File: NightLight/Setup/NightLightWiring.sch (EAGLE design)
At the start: 19 parts

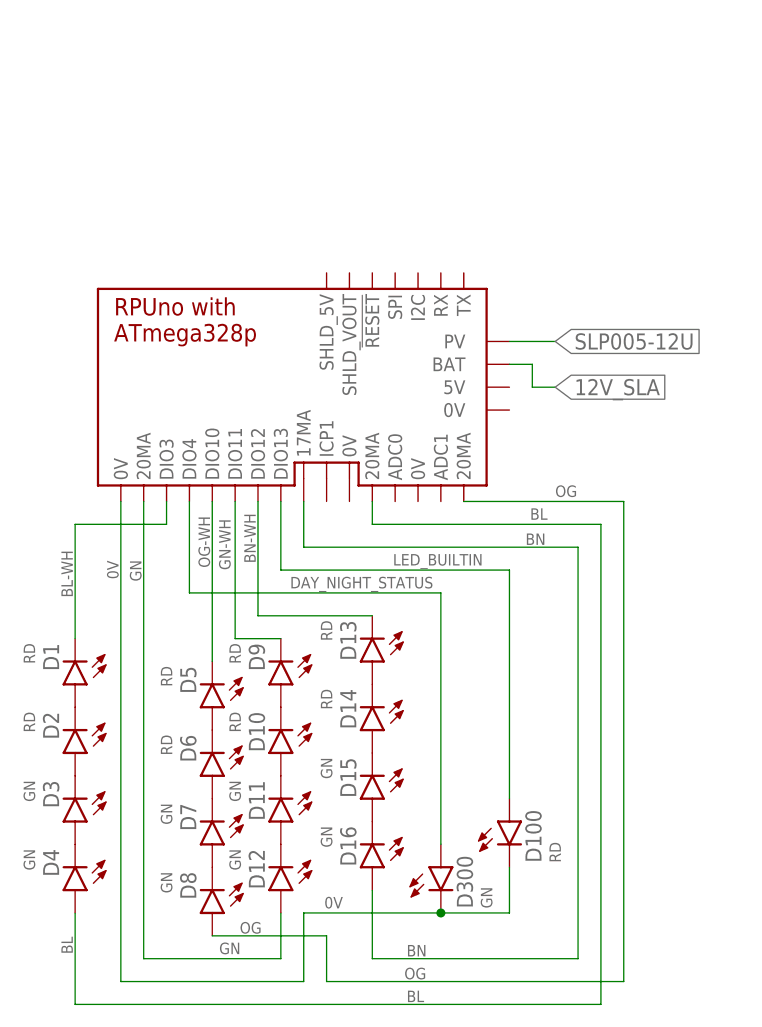
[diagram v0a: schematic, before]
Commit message: NightLight: evaluation
100 Ohm added to status led
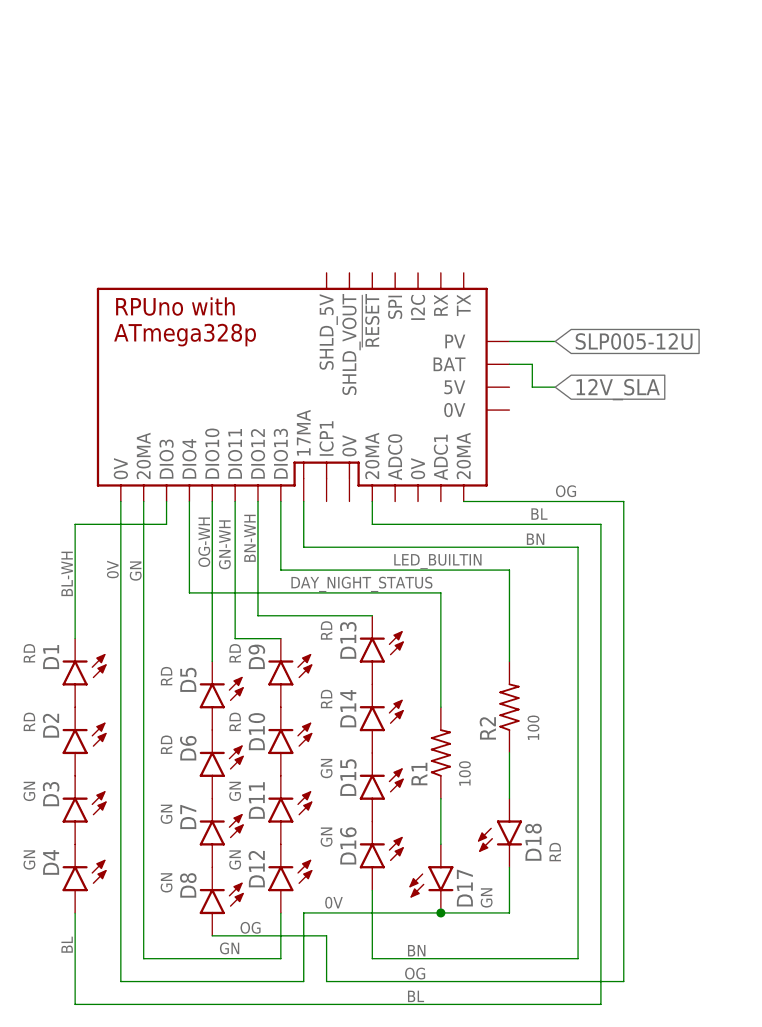
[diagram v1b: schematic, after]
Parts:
- added R1, R2: 100, R-C:R0805
- renumbered D100 to D18, D300 to D17
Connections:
- new net N$1: D17.A, R1.1
- new net N$2: D18.A, R2.1
- net DAY_NIGHT_STATUS: now also R1.2; no longer D17.A
- net LED_BUILTIN: now also R2.2; no longer D18.A
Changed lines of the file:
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@@
 <parts>
 <part name="BM3" library="Documentation" deviceset="RPUNO" device=""/>
-<part name="D100" library="D-LED" deviceset="LED" device="5MM" value="RD"/>
-<part name="D300" library="D-LED" deviceset="LED" device="5MM" value="GN"/>
+<part name="D18" library="D-LED" deviceset="LED" device="5MM" value="RD"/>
+<part name="D17" library="D-LED" deviceset="LED" device="5MM" value="GN"/>
 <part name="D1" library="D-LED" deviceset="LED" device="5MM" value="RD"/>
 <part name="D2" library="D-LED" deviceset="LED" device="5MM" value="RD"/>
@@
 <part name="D15" library="D-LED" deviceset="LED" device="5MM" value="GN"/>
 <part name="D16" library="D-LED" deviceset="LED" device="5MM" value="GN"/>
+<part name="R1" library="R-C" deviceset="R" device="0805" value="100"/>
+<part name="R2" library="R-C" deviceset="R" device="0805" value="100"/>
 </parts>
 <sheets>
@@
 <instances>
 <instance part="BM3" gate="G$1" x="45.72" y="109.22"/>
-<instance part="D100" gate="G$1" x="66.04" y="58.42"/>
-<instance part="D300" gate="G$1" x="58.42" y="53.34"/>
+<instance part="D18" gate="G$1" x="66.04" y="58.42"/>
+<instance part="D17" gate="G$1" x="58.42" y="53.34"/>
 <instance part="D1" gate="G$1" x="17.78" y="73.66" rot="R180"/>
 <instance part="D2" gate="G$1" x="17.78" y="66.04" rot="R180"/>
@@
 <instance part="D15" gate="G$1" x="50.8" y="60.96" rot="R180"/>
 <instance part="D16" gate="G$1" x="50.8" y="53.34" rot="R180"/>
+<instance part="R1" gate="G$1" x="58.42" y="66.04" rot="R90"/>
+<instance part="R2" gate="G$1" x="66.04" y="71.12" rot="R90"/>
 </instances>
 <busses>
@@
 <segment>
 <pinref part="BM3" gate="G$1" pin="DIO4"/>
-<wire x1="58.42" y1="55.88" x2="58.42" y2="83.82" width="0.1524" layer="91"/>
+<wire x1="58.42" y1="71.12" x2="58.42" y2="83.82" width="0.1524" layer="91"/>
 <wire x1="58.42" y1="83.82" x2="30.48" y2="83.82" width="0.1524" layer="91"/>
 <wire x1="30.48" y1="83.82" x2="30.48" y2="93.98" width="0.1524" layer="91"/>
-<pinref part="D300" gate="G$1" pin="A"/>
 <label x="41.656" y="84.328" size="1.27" layer="91"/>
+<pinref part="R1" gate="G$1" pin="2"/>
 </segment>
 </net>
@@
 <segment>
 <pinref part="BM3" gate="G$1" pin="DIO13"/>
-<pinref part="D100" gate="G$1" pin="A"/>
 <wire x1="40.64" y1="93.98" x2="40.64" y2="86.36" width="0.1524" layer="91"/>
 <wire x1="40.64" y1="86.36" x2="66.04" y2="86.36" width="0.1524" layer="91"/>
-<wire x1="66.04" y1="86.36" x2="66.04" y2="60.96" width="0.1524" layer="91"/>
+<wire x1="66.04" y1="86.36" x2="66.04" y2="76.2" width="0.1524" layer="91"/>
 <label x="53.086" y="86.868" size="1.27" layer="91"/>
+<pinref part="R2" gate="G$1" pin="2"/>
 </segment>
 </net>
 <net name="0V" class="0">
 <segment>
-<pinref part="D100" gate="G$1" pin="K"/>
+<pinref part="D18" gate="G$1" pin="K"/>
 <wire x1="66.04" y1="53.34" x2="66.04" y2="48.26" width="0.1524" layer="91"/>
 <wire x1="66.04" y1="48.26" x2="58.42" y2="48.26" width="0.1524" layer="91"/>
-<pinref part="D300" gate="G$1" pin="K"/>
+<pinref part="D17" gate="G$1" pin="K"/>
 <pinref part="BM3" gate="G$1" pin="0V@3"/>
 <wire x1="22.86" y1="93.98" x2="22.86" y2="40.64" width="0.1524" layer="91"/>
@@
 </segment>
 </net>
+<net name="N$1" class="0">
+<segment>
+<pinref part="D17" gate="G$1" pin="A"/>
+<pinref part="R1" gate="G$1" pin="1"/>
+<wire x1="58.42" y1="60.96" x2="58.42" y2="55.88" width="0.1524" layer="91"/>
+</segment>
+</net>
+<net name="N$2" class="0">
+<segment>
+<pinref part="D18" gate="G$1" pin="A"/>
+<pinref part="R2" gate="G$1" pin="1"/>
+<wire x1="66.04" y1="66.04" x2="66.04" y2="60.96" width="0.1524" layer="91"/>
+</segment>
+</net>

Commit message: NightLight: ^9 updates
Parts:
- removed R1, R2: 100, R-C:R0805
- added D19: RD, D-LED:LED5MM
- D11, D12, D15, D16, D3, D4, D7, D8: value GN -> RD
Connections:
- removed net DAY_NIGHT_STATUS: BM3.DIO4, R1.2
- removed net LED_BUILTIN: BM3.DIO13, R2.2
- removed net N$1: D17.A, R1.1
- removed net N$2: D18.A, R2.1
- new net DAYNIGHT_STATUS_LED: BM3.DIO12, D17.A
- new net LIGHT_SENSOR: BM3.ADC2_16, D19.K
- new net STATUS_LED: BM3.DIO13, D18.A
- net 0V: no longer BM3.0V@3
- net 12V_SLA: now also BM3.PWR; no longer BM3.BAT
- net BL: now also BM3.CS0_EN5; no longer BM3.20MA@0
- net BL-WH: now also BM3.0V@3; no longer BM3.DIO3
- net BN: now also BM3.CS3_EN4; no longer BM3.17MA@0
- net BN-WH: now also BM3.0V@6; no longer BM3.DIO12
- net GN: now also BM3.CS2_EN3; no longer BM3.20MA@2
- net GN-WH: now also BM3.0V@5, D19.A; no longer BM3.DIO11
- net OG: now also BM3.CS1_EN6; no longer BM3.20MA@1
- net OG-WH: no longer BM3.DIO10
- net SLP005-12U: now also BM3.ALT; no longer BM3.PV
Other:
- moved on the sheet: D1, D10, D11, D12, D13, D14, D15, D16, D17, D18, D2, D3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

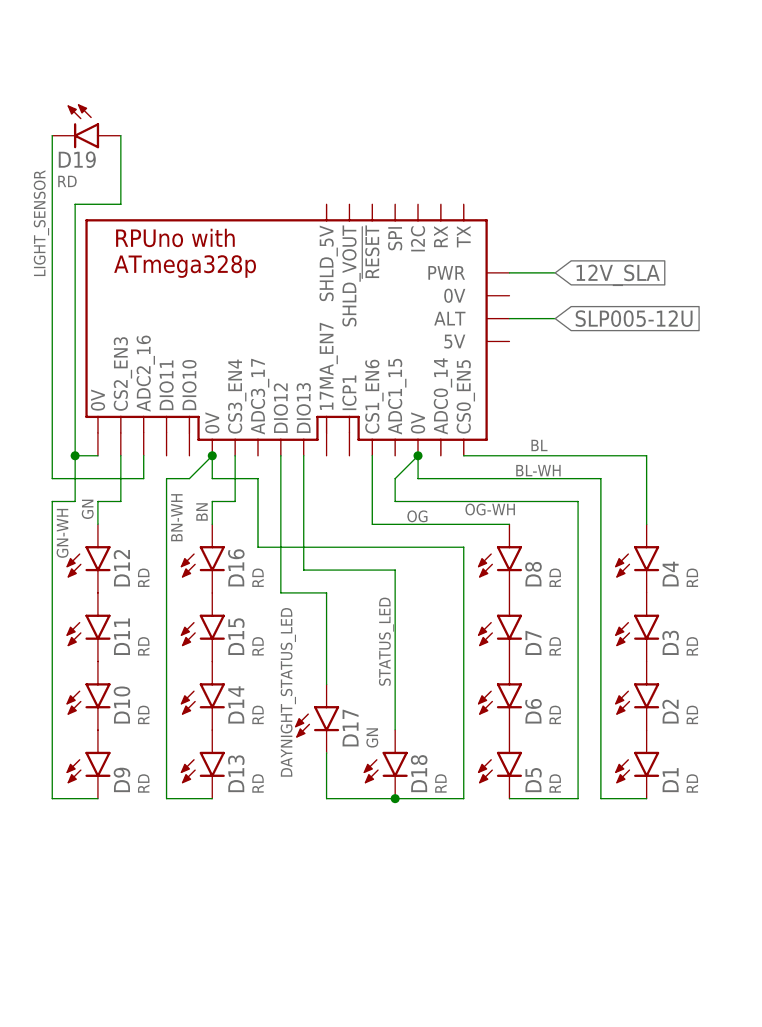
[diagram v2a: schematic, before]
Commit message: Reflow: ^9 updates and add a light sensor to start profile
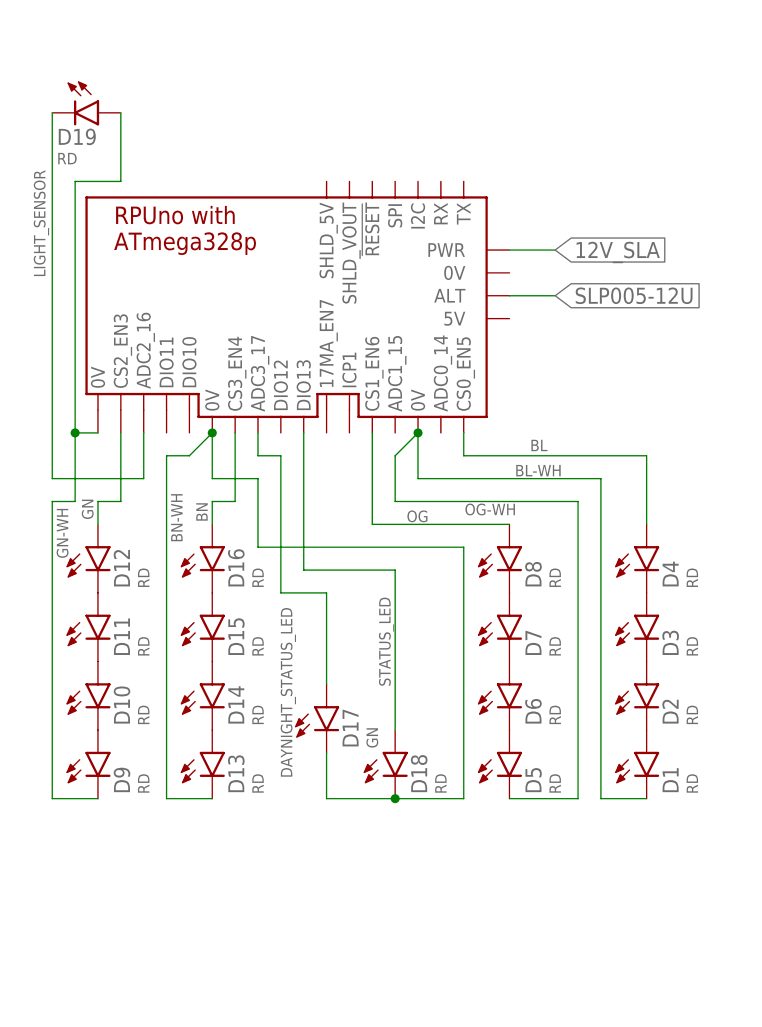
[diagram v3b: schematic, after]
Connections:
- net DAYNIGHT_STATUS_LED: now also BM3.ADC3_17; no longer BM3.DIO12
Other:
- moved on the sheet: D19
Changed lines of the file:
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@@
 </plain>
 <instances>
-<instance part="BM3" gate="G$1" x="45.72" y="114.3"/>
+<instance part="BM3" gate="G$1" x="45.72" y="116.84"/>
 <instance part="D18" gate="G$1" x="53.34" y="66.04"/>
 <instance part="D17" gate="G$1" x="45.72" y="71.12"/>
@@
 <instance part="D15" gate="G$1" x="33.02" y="81.28"/>
 <instance part="D16" gate="G$1" x="33.02" y="88.9"/>
-<instance part="D19" gate="G$1" x="20.32" y="134.62" rot="R270"/>
+<instance part="D19" gate="G$1" x="20.32" y="137.16" rot="R270"/>
 </instances>
 <busses>
@@
 <net name="SLP005-12U" class="0">
 <segment>
-<label x="71.12" y="114.3" size="1.778" layer="91" xref="yes"/>
+<label x="71.12" y="116.84" size="1.778" layer="91" xref="yes"/>
 <pinref part="BM3" gate="G$1" pin="ALT"/>
-<wire x1="71.12" y1="114.3" x2="66.04" y2="114.3" width="0.1524" layer="91"/>
+<wire x1="71.12" y1="116.84" x2="66.04" y2="116.84" width="0.1524" layer="91"/>
 </segment>
 </net>
 <net name="12V_SLA" class="0">
 <segment>
-<label x="71.12" y="119.38" size="1.778" layer="91" xref="yes"/>
+<label x="71.12" y="121.92" size="1.778" layer="91" xref="yes"/>
 <pinref part="BM3" gate="G$1" pin="PWR"/>
-<wire x1="71.12" y1="119.38" x2="66.04" y2="119.38" width="0.1524" layer="91"/>
+<wire x1="71.12" y1="121.92" x2="66.04" y2="121.92" width="0.1524" layer="91"/>
 </segment>
 </net>
@@
 <wire x1="40.64" y1="83.82" x2="40.64" y2="99.06" width="0.1524" layer="91"/>
 <label x="41.91" y="63.246" size="1.27" layer="91" rot="R90"/>
-<pinref part="BM3" gate="G$1" pin="DIO12"/>
 <pinref part="D17" gate="G$1" pin="A"/>
+<pinref part="BM3" gate="G$1" pin="ADC3_17"/>
+<wire x1="38.1" y1="101.6" x2="38.1" y2="99.06" width="0.1524" layer="91"/>
+<wire x1="38.1" y1="99.06" x2="40.64" y2="99.06" width="0.1524" layer="91"/>
 </segment>
 </net>
@@
 <label x="52.832" y="73.406" size="1.27" layer="91" rot="R90"/>
 <pinref part="BM3" gate="G$1" pin="DIO13"/>
-<wire x1="43.18" y1="86.36" x2="43.18" y2="99.06" width="0.1524" layer="91"/>
+<wire x1="43.18" y1="86.36" x2="43.18" y2="101.6" width="0.1524" layer="91"/>
 <pinref part="D18" gate="G$1" pin="A"/>
 </segment>
@@
 <wire x1="38.1" y1="88.9" x2="38.1" y2="96.52" width="0.1524" layer="91"/>
 <wire x1="38.1" y1="96.52" x2="33.02" y2="96.52" width="0.1524" layer="91"/>
-<wire x1="33.02" y1="96.52" x2="33.02" y2="98.552" width="0.1524" layer="91"/>
+<wire x1="33.02" y1="96.52" x2="33.02" y2="101.092" width="0.1524" layer="91"/>
 </segment>
 </net>
@@
 <pinref part="BM3" gate="G$1" pin="0V@3"/>
 <wire x1="76.2" y1="96.52" x2="55.88" y2="96.52" width="0.1524" layer="91"/>
-<wire x1="55.88" y1="96.52" x2="55.88" y2="99.06" width="0.1524" layer="91"/>
-<wire x1="55.88" y1="99.06" x2="55.626" y2="99.06" width="0.1524" layer="91"/>
-<junction x="55.88" y="99.06"/>
+<wire x1="55.88" y1="96.52" x2="55.88" y2="101.6" width="0.1524" layer="91"/>
+<wire x1="55.88" y1="101.6" x2="55.626" y2="101.6" width="0.1524" layer="91"/>
+<junction x="55.88" y="101.6"/>
 </segment>
 </net>
@@
 <wire x1="81.28" y1="91.44" x2="81.28" y2="99.06" width="0.1524" layer="91"/>
 <wire x1="81.28" y1="99.06" x2="60.96" y2="99.06" width="0.1524" layer="91"/>
+<wire x1="60.96" y1="99.06" x2="60.96" y2="101.6" width="0.1524" layer="91"/>
 <label x="68.326" y="99.568" size="1.27" layer="91"/>
 <pinref part="BM3" gate="G$1" pin="CS0_EN5"/>
@@
 <wire x1="73.66" y1="60.96" x2="73.66" y2="93.98" width="0.1524" layer="91"/>
 <wire x1="73.66" y1="93.98" x2="53.34" y2="93.98" width="0.1524" layer="91"/>
-<wire x1="53.34" y1="93.98" x2="53.34" y2="96.52" width="0.1524" layer="91"/>
-<wire x1="53.34" y1="96.52" x2="55.626" y2="98.806" width="0.1524" layer="91"/>
+<wire x1="53.34" y1="93.98" x2="53.34" y2="99.06" width="0.1524" layer="91"/>
+<wire x1="53.34" y1="99.06" x2="55.626" y2="101.346" width="0.1524" layer="91"/>
 </segment>
 </net>
@@
 <pinref part="BM3" gate="G$1" pin="CS1_EN6"/>
 <wire x1="66.04" y1="91.44" x2="50.8" y2="91.44" width="0.1524" layer="91"/>
-<wire x1="50.8" y1="91.44" x2="50.8" y2="99.06" width="0.1524" layer="91"/>
+<wire x1="50.8" y1="91.44" x2="50.8" y2="101.6" width="0.1524" layer="91"/>
 </segment>
 </net>
@@
 <wire x1="15.24" y1="60.96" x2="15.24" y2="93.98" width="0.1524" layer="91"/>
 <wire x1="15.24" y1="93.98" x2="17.78" y2="93.98" width="0.1524" layer="91"/>
-<wire x1="17.78" y1="93.98" x2="17.78" y2="99.06" width="0.1524" layer="91"/>
+<wire x1="17.78" y1="93.98" x2="17.78" y2="101.6" width="0.1524" layer="91"/>
 <pinref part="BM3" gate="G$1" pin="0V@5"/>
-<wire x1="17.78" y1="99.06" x2="20.32" y2="99.06" width="0.1524" layer="91"/>
+<wire x1="17.78" y1="101.6" x2="20.32" y2="101.6" width="0.1524" layer="91"/>
 <pinref part="D19" gate="G$1" pin="A"/>
-<wire x1="22.86" y1="134.62" x2="22.86" y2="127" width="0.1524" layer="91"/>
-<wire x1="22.86" y1="127" x2="17.78" y2="127" width="0.1524" layer="91"/>
-<wire x1="17.78" y1="127" x2="17.78" y2="99.06" width="0.1524" layer="91"/>
-<junction x="17.78" y="99.06"/>
+<wire x1="22.86" y1="137.16" x2="22.86" y2="129.54" width="0.1524" layer="91"/>
+<wire x1="22.86" y1="129.54" x2="17.78" y2="129.54" width="0.1524" layer="91"/>
+<wire x1="17.78" y1="129.54" x2="17.78" y2="101.6" width="0.1524" layer="91"/>
+<junction x="17.78" y="101.6"/>
 </segment>
 </net>
@@
 <wire x1="33.02" y1="60.96" x2="27.94" y2="60.96" width="0.1524" layer="91"/>
 <label x="29.718" y="89.408" size="1.27" layer="91" rot="R90"/>
-<wire x1="27.94" y1="60.96" x2="27.94" y2="96.52" width="0.1524" layer="91"/>
-<wire x1="27.94" y1="96.52" x2="30.48" y2="96.52" width="0.1524" layer="91"/>
+<wire x1="27.94" y1="60.96" x2="27.94" y2="99.06" width="0.1524" layer="91"/>
+<wire x1="27.94" y1="99.06" x2="30.48" y2="99.06" width="0.1524" layer="91"/>
 <pinref part="BM3" gate="G$1" pin="0V@6"/>
-<wire x1="30.48" y1="96.52" x2="33.02" y2="99.06" width="0.1524" layer="91"/>
-<wire x1="33.02" y1="99.06" x2="33.274" y2="99.06" width="0.1524" layer="91"/>
-<junction x="33.02" y="99.06"/>
+<wire x1="30.48" y1="99.06" x2="33.02" y2="101.6" width="0.1524" layer="91"/>
+<wire x1="33.02" y1="101.6" x2="33.274" y2="101.6" width="0.1524" layer="91"/>
+<junction x="33.02" y="101.6"/>
 </segment>
 </net>
@@
 <segment>
 <pinref part="D12" gate="G$1" pin="A"/>
-<wire x1="22.86" y1="99.06" x2="22.86" y2="93.98" width="0.1524" layer="91"/>
+<wire x1="22.86" y1="101.6" x2="22.86" y2="93.98" width="0.1524" layer="91"/>
 <wire x1="22.86" y1="93.98" x2="20.32" y2="93.98" width="0.1524" layer="91"/>
 <wire x1="20.32" y1="93.98" x2="20.32" y2="91.44" width="0.1524" layer="91"/>
@@
 <wire x1="33.02" y1="91.44" x2="33.02" y2="93.98" width="0.1524" layer="91"/>
 <wire x1="33.02" y1="93.98" x2="35.56" y2="93.98" width="0.1524" layer="91"/>
-<wire x1="35.56" y1="93.98" x2="35.56" y2="99.06" width="0.1524" layer="91"/>
+<wire x1="35.56" y1="93.98" x2="35.56" y2="101.6" width="0.1524" layer="91"/>
 <label x="32.512" y="91.694" size="1.27" layer="91" rot="R90"/>
 <pinref part="BM3" gate="G$1" pin="CS3_EN4"/>
@@
 <segment>
 <pinref part="D19" gate="G$1" pin="K"/>
-<wire x1="15.24" y1="134.62" x2="15.24" y2="96.52" width="0.1524" layer="91"/>
+<wire x1="15.24" y1="137.16" x2="15.24" y2="96.52" width="0.1524" layer="91"/>
 <wire x1="15.24" y1="96.52" x2="25.4" y2="96.52" width="0.1524" layer="91"/>
 <pinref part="BM3" gate="G$1" pin="ADC2_16"/>
-<wire x1="25.4" y1="96.52" x2="25.4" y2="99.06" width="0.1524" layer="91"/>
+<wire x1="25.4" y1="96.52" x2="25.4" y2="101.6" width="0.1524" layer="91"/>
 <label x="14.478" y="118.872" size="1.27" layer="91" rot="R90"/>
 </segment>

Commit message: Solenoid: wiring show flow sensor
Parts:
- added R1: 100k, R-C:R0805
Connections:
- net GN-WH: now also R1.1
- net LIGHT_SENSOR: now also R1.2
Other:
- moved on the sheet: D19
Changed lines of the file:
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@@
 <part name="D16" library="D-LED" deviceset="LED" device="5MM" value="RD"/>
 <part name="D19" library="D-LED" deviceset="LED" device="5MM" value="RD"/>
+<part name="R1" library="R-C" deviceset="R" device="0805" value="100k"/>
 </parts>
 <sheets>
@@
 <instance part="D15" gate="G$1" x="33.02" y="81.28"/>
 <instance part="D16" gate="G$1" x="33.02" y="88.9"/>
-<instance part="D19" gate="G$1" x="20.32" y="137.16" rot="R270"/>
+<instance part="D19" gate="G$1" x="20.32" y="142.24" rot="R270"/>
+<instance part="R1" gate="G$1" x="20.32" y="134.62" rot="R180"/>
 </instances>
 <busses>
@@
 <wire x1="17.78" y1="101.6" x2="20.32" y2="101.6" width="0.1524" layer="91"/>
 <pinref part="D19" gate="G$1" pin="A"/>
-<wire x1="22.86" y1="137.16" x2="22.86" y2="129.54" width="0.1524" layer="91"/>
-<wire x1="22.86" y1="129.54" x2="17.78" y2="129.54" width="0.1524" layer="91"/>
+<wire x1="22.86" y1="142.24" x2="25.4" y2="142.24" width="0.1524" layer="91"/>
+<wire x1="25.4" y1="142.24" x2="25.4" y2="134.62" width="0.1524" layer="91"/>
+<wire x1="25.4" y1="134.62" x2="25.4" y2="129.54" width="0.1524" layer="91"/>
+<wire x1="25.4" y1="129.54" x2="17.78" y2="129.54" width="0.1524" layer="91"/>
 <wire x1="17.78" y1="129.54" x2="17.78" y2="101.6" width="0.1524" layer="91"/>
 <junction x="17.78" y="101.6"/>
+<pinref part="R1" gate="G$1" pin="1"/>
+<junction x="25.4" y="134.62"/>
 </segment>
 </net>
@@
 <segment>
 <pinref part="D19" gate="G$1" pin="K"/>
-<wire x1="15.24" y1="137.16" x2="15.24" y2="96.52" width="0.1524" layer="91"/>
+<wire x1="15.24" y1="142.24" x2="15.24" y2="134.62" width="0.1524" layer="91"/>
+<wire x1="15.24" y1="134.62" x2="15.24" y2="96.52" width="0.1524" layer="91"/>
 <wire x1="15.24" y1="96.52" x2="25.4" y2="96.52" width="0.1524" layer="91"/>
 <pinref part="BM3" gate="G$1" pin="ADC2_16"/>
 <wire x1="25.4" y1="96.52" x2="25.4" y2="101.6" width="0.1524" layer="91"/>
 <label x="14.478" y="118.872" size="1.27" layer="91" rot="R90"/>
-</segment>
-</net>
+<pinref part="R1" gate="G$1" pin="2"/>
+<junction x="15.24" y="134.62"/>
+</segment>
+</net>
